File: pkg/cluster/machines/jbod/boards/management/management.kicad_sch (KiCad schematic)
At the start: 48 parts, among them J1 PSU_L, J10 FAN5, J11 FAN6, J12 I2C, J13 Conn_01x02, J2 FAN1, J3 SAS_L, J4 SAS_R, J5 LED, J6 PSU_R, J7 FAN2, J8 FAN3, J9 FAN4, Q1 2N7002, Q2 2N7002, Q3 DMG2301L, Q4 DMG2301L, U1 SN74AHCT125DR, U2 NRF52840_ITSY_BITSY, U3 AGQ20012

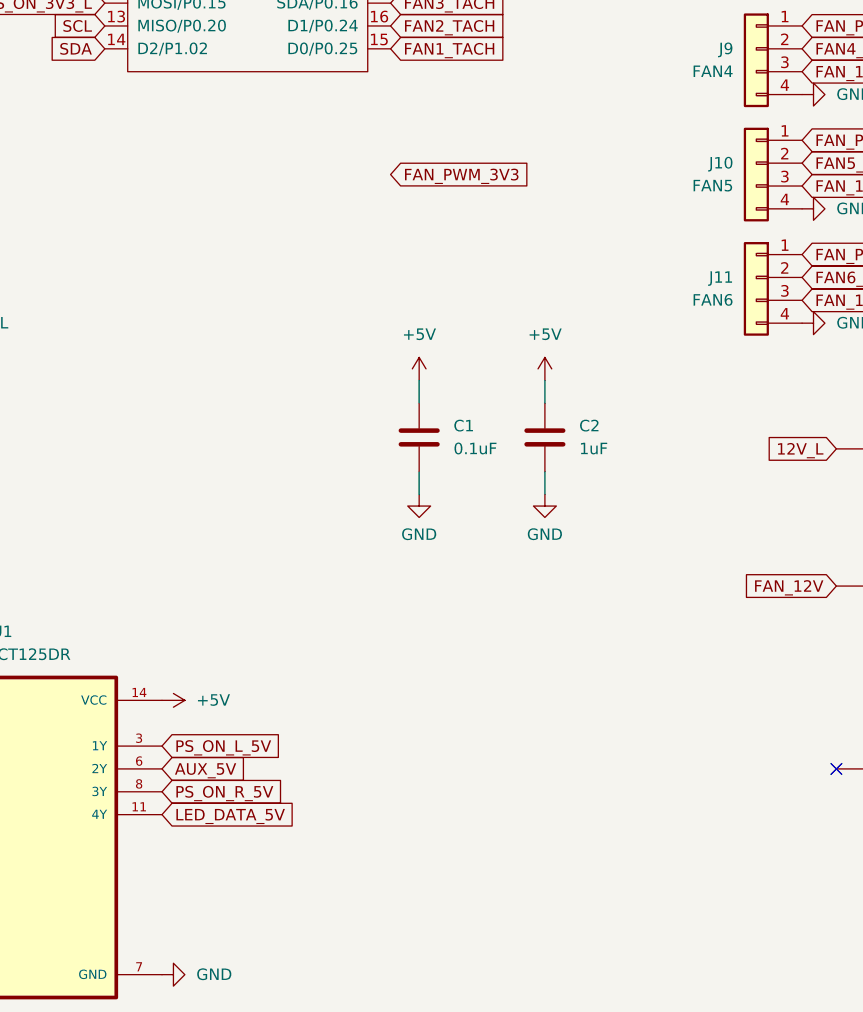
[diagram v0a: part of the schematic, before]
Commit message: Add cluster blob replication and separate resolver service.
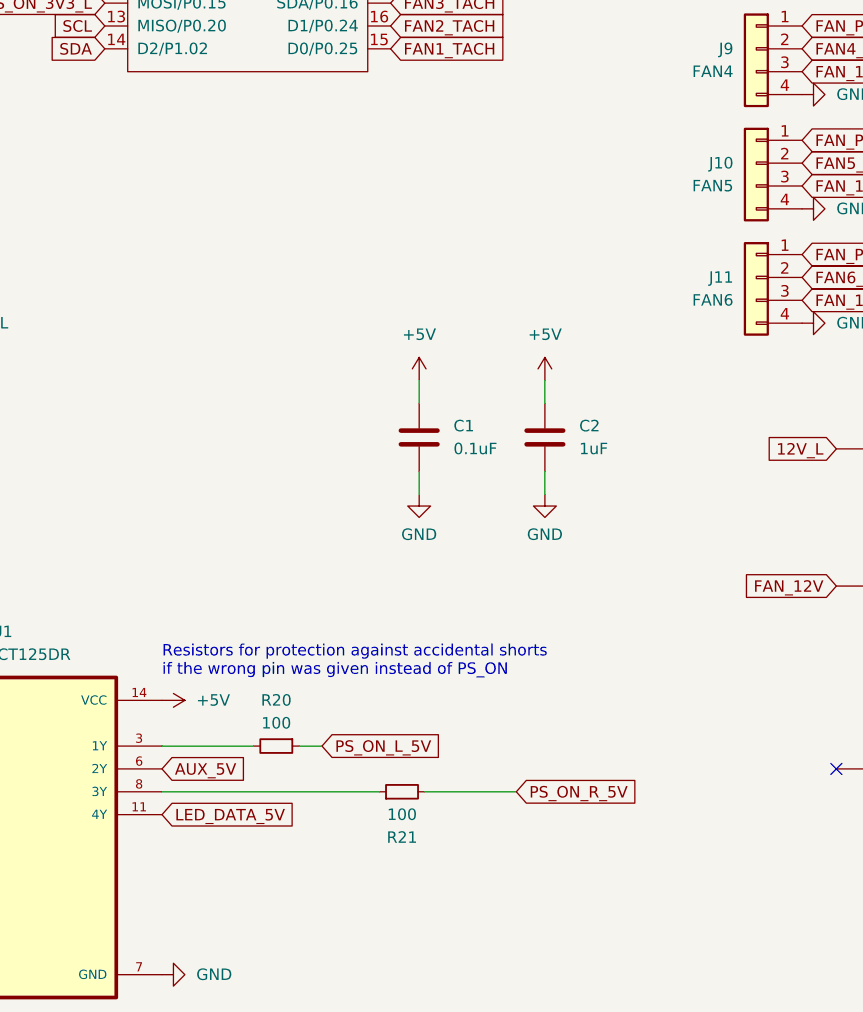
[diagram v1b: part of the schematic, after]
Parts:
- added R20, R21: 100, Resistor_SMD:R_0805_2012Metric_Pad1.20x1.40mm_HandSolder, symbol Device:R_Small
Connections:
- net PS_ON_L_5V: now also R20.1; no longer U1.3 (1Y)
- net PS_ON_R_5V: now also R21.2; no longer U1.8 (3Y)
- new net: R20.2, U1.3 (1Y)
- new net: R21.1, U1.8 (3Y)
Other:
- note added: "Resistors for protection against accidental shorts if the wrong pin was given instead of PS_ON"
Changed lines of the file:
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@@
+    (stroke (width 0) (type default))
+  )
+  (wire (pts (xy 148.59 151.13) (xy 158.75 151.13))
     (stroke (width 0) (type default))
   )
@@
     (stroke (width 0) (type default))
   )
+  (wire (pts (xy 163.83 151.13) (xy 166.37 151.13))
+    (stroke (width 0) (type default))
+  )
   (wire (pts (xy 97.79 151.13) (xy 110.49 151.13))
     (stroke (width 0) (type default))
@@
     (stroke (width 0) (type default))
   )
+  (wire (pts (xy 177.8 156.21) (xy 187.96 156.21))
+    (stroke (width 0) (type default))
+  )
   (wire (pts (xy 266.7 73.66) (xy 270.51 73.66))
     (stroke (width 0) (type default))
@@
     (stroke (width 0) (type default))
   )
+  (wire (pts (xy 148.59 156.21) (xy 172.72 156.21))
+    (stroke (width 0) (type default))
+  )
   (wire (pts (xy 255.27 45.72) (xy 259.08 45.72))
     (stroke (width 0) (type default))
@@
   (wire (pts (xy 266.7 31.75) (xy 270.51 31.75))
     (stroke (width 0) (type default))
+  )
+  (text "Resistors for protection against accidental shorts\nif the wrong pin was given instead of PS_ON"
+    (at 148.59 143.51 0)
+    (effects (font (size 1.27 1.27)) (justify left bottom))
   )
   (text "All fan power with run from the left PSU\nsince it has one less disk"
@@
     )
   )
-  (global_label "PS_ON_L_5V" (shape input) (at 148.59 151.13 0) (fields_autoplaced)
-    (effects (font (size 1.27 1.27)) (justify left))
-    (property "Intersheetrefs" "${INTERSHEET_REFS}" (at 162.9447 151.13 0)
+  (global_label "PS_ON_L_5V" (shape input) (at 166.37 151.13 0) (fields_autoplaced)
+    (effects (font (size 1.27 1.27)) (justify left))
+    (property "Intersheetrefs" "${INTERSHEET_REFS}" (at 180.7247 151.13 0)
       (effects (font (size 1.27 1.27)) (justify left) hide)
     )
@@
     )
   )
-  (global_label "FAN_PWM_3V3" (shape input) (at 173.99 87.63 0) (fields_autoplaced)
-    (effects (font (size 1.27 1.27)) (justify left))
-    (property "Intersheetrefs" "${INTERSHEET_REFS}" (at 190.0985 87.63 0)
-      (effects (font (size 1.27 1.27)) (justify left) hide)
-    )
-  )
   (global_label "FAN_PWM_5V" (shape input) (at 219.71 29.21 0) (fields_autoplaced)
     (effects (font (size 1.27 1.27)) (justify left))
@@
     )
   )
-  (global_label "PS_ON_R_5V" (shape input) (at 148.59 156.21 0) (fields_autoplaced)
-    (effects (font (size 1.27 1.27)) (justify left))
-    (property "Intersheetrefs" "${INTERSHEET_REFS}" (at 163.1866 156.21 0)
+  (global_label "PS_ON_R_5V" (shape input) (at 187.96 156.21 0) (fields_autoplaced)
+    (effects (font (size 1.27 1.27)) (justify left))
+    (property "Intersheetrefs" "${INTERSHEET_REFS}" (at 202.5566 156.21 0)
       (effects (font (size 1.27 1.27)) (justify left) hide)
     )
@@
     )
   )
+  (symbol (lib_id "Device:R_Small") (at 161.29 151.13 270) (unit 1)
+    (in_bom yes) (on_board yes) (dnp no)
+    (property "Reference" "R20" (at 161.29 146.05 90)
+      (effects (font (size 1.27 1.27)))
+    )
+    (property "Value" "100" (at 161.29 148.59 90)
+      (effects (font (size 1.27 1.27)))
+    )
+    (property "Footprint" "Resistor_SMD:R_0805_2012Metric_Pad1.20x1.40mm_HandSolder" (at 161.29 151.13 0)
+      (effects (font (size 1.27 1.27)) hide)
+    )
+    (property "Datasheet" "~" (at 161.29 151.13 0)
+      (effects (font (size 1.27 1.27)) hide)
+    )
+    (pin "1")
+    (pin "2")
+    (instances
+      (project "management"
+        (path "/e83f4817-5adf-4616-a9be-8001639a376c"
+          (reference "R20") (unit 1)
+        )
+      )
+    )
+  )
   (symbol (lib_id "power:GND") (at 93.98 77.47 0) (unit 1)
     (in_bom yes) (on_board yes) (dnp no) (fields_autoplaced)
@@
         )
       )
+    )
+  )
+  (symbol (lib_id "Device:R_Small") (at 175.26 156.21 90) (unit 1)
+    (in_bom yes) (on_board yes) (dnp no)
+    (property "Reference" "R21" (at 175.26 161.29 90)
+      (effects (font (size 1.27 1.27)))
+    )
+    (property "Value" "100" (at 175.26 158.75 90)
+      (effects (font (size 1.27 1.27)))
+    )
+    (property "Footprint" "Resistor_SMD:R_0805_2012Metric_Pad1.20x1.40mm_HandSolder" (at 175.26 156.21 0)
+      (effects (font (size 1.27 1.27)) hide)
+    )
+    (property "Datasheet" "~" (at 175.26 156.21 0)
+      (effects (font (size 1.27 1.27)) hide)
+    )
+    (pin "1")
+    (pin "2")
+    (instances
+      (project "management"
+        (path "/e83f4817-5adf-4616-a9be-8001639a376c"
+          (reference "R21") (unit 1)
+        )
+      )
